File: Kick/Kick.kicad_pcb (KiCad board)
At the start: 4 copper layers, 11 parts, among them J1 CN1 / J11, J2 CN2 / J12, U0 NOIP1SN1300A-QTI, U1 NOIP1SN1300A-QTI, U2 NX3L4053, U3 NX3L4053, U4 MIC5504-1.8YM5

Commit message: acurrate placement of devices, HF impedance calculation
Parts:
- moved U3 12.4 mm to (118.7, 87.6)
- moved U0 11.2 mm to (104.4, 69.4)
- moved U2 10.9 mm to (86.8, 89.4)
- moved U1 9.72 mm to (78.3, 69.4)
- moved J2 2.58 mm to (97.1, 49.2)
- moved J1 2.34 mm to (96.1, 102.2)
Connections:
- J2 pad 22: /clkoutp_0 -> /clkout0_N
- J2 pad 24: /clkoutn_0 -> /clkout0_P
- J2 pad 26: /doutp0_0 -> /dout0_0_N
- J2 pad 28: /doutn0_0 -> /dout0_0_P
- J2 pad 32: /doutp1_0 -> /dout1_0_N
- J2 pad 34: /doutn1_0 -> /dout1_0_P
- J2 pad 36: /doutp2_0 -> /dout2_0_N
- J2 pad 38: /doutn2_0 -> /dout2_0_P
- J2 pad 42: /doutp3_0 -> /dout3_0_N
- J2 pad 44: /doutn3_0 -> /dout3_0_P
- J2 pad 46: /syncp_0 -> /sync0_N
- J2 pad 48: /syncn_0 -> /sync0_P
- J2 pad 52: /clkoutp_1 -> /clkout1_N
- J2 pad 54: /clkoutn_1 -> /clkout1_P
- J2 pad 56: /doutp0_1 -> /dout0_1_N
- J2 pad 58: /doutn0_1 -> /dout0_1_P
- J2 pad 62: /doutp1_1 -> /dout1_1_N
- J2 pad 64: /doutn1_1 -> /dout1_1_P
- J2 pad 66: /doutp2_1 -> /dout2_1_N
- J2 pad 68: /doutn2_1 -> /dout2_1_P
- J2 pad 72: /doutp3_1 -> /dout3_1_N
- J2 pad 74: /doutn3_1 -> /dout3_1_P
- J2 pad 76: /syncp_1 -> /sync1_N
- J2 pad 78: /syncn_1 -> /sync1_P
- U0 pad 10: /doutp0_0 -> /dout0_0_P
- U0 pad 11: /doutn1_0 -> /dout1_0_N
- U0 pad 12: /doutp1_0 -> /dout1_0_P
- U0 pad 13: /doutn2_0 -> /dout2_0_N
- U0 pad 14: /doutp2_0 -> /dout2_0_P
- U0 pad 15: /doutn3_0 -> /dout3_0_N
- U0 pad 16: /doutp3_0 -> /dout3_0_P
- U0 pad 17: /syncn_0 -> /sync0_N
- U0 pad 18: /syncp_0 -> /sync0_P
- U0 pad 46: /resetn_0 -> /reset0_N
- U0 pad 7: /clkoutn_0 -> /clkout0_N
- U0 pad 8: /clkoutp_0 -> /clkout0_P
- U0 pad 9: /doutn0_0 -> /dout0_0_N
- U1 pad 10: /doutp0_1 -> /dout0_1_P
- U1 pad 11: /doutn1_1 -> /dout1_1_N
- U1 pad 12: /doutp1_1 -> /dout1_1_P
- U1 pad 13: /doutn2_1 -> /dout2_1_N
- U1 pad 14: /doutp2_1 -> /dout2_1_P
- U1 pad 15: /doutn3_1 -> /dout3_1_N
- U1 pad 16: /doutp3_1 -> /dout3_1_P
- U1 pad 17: /syncn_1 -> /sync1_N
- U1 pad 18: /syncp_1 -> /sync1_P
- U1 pad 7: /clkoutn_1 -> /clkout1_N
- U1 pad 8: /clkoutp_1 -> /clkout1_P
- U1 pad 9: /doutn0_1 -> /dout0_1_N
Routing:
- net /sync1_P: track 0.00 -> 5.84 mm
- net /sync1_N: track 0.00 -> 5.84 mm

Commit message: calculated new, thinner track widths for 7628 stackup.
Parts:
- moved C1 7.21 mm to (122.1, 72.5)
- moved C2 7.21 mm to (123.5, 68.0)
- moved R1 7.21 mm to (123.5, 70.5)
- moved R2 7.21 mm to (123.5, 73.0)
- moved U4 7.21 mm to (118.9, 66.7)
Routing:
- net /sync1_P: track 5.84 -> 0.00 mm
- net /sync1_N: track 5.84 -> 0.00 mm
- added copper zone on In1.Cu, net GND
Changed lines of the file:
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@@
 	(layers
 		(0 "F.Cu" signal)
-		(1 "In1.Cu" signal)
-		(2 "In2.Cu" signal)
+		(1 "In1.Cu" power)
+		(2 "In2.Cu" power)
 		(31 "B.Cu" signal)
 		(32 "B.Adhes" user "B.Adhesive")
@@
 		(pad_to_mask_clearance 0)
 		(allow_soldermask_bridges_in_footprints no)
-		(grid_origin 70.845 43.925)
+		(grid_origin 65 44)
 		(pcbplotparams
 			(layerselection 0x00010fc_ffffffff)
@@
 	(footprint "Resistor_SMD:R_0603_1608Metric"
 		(layer "B.Cu")
-		(at 130.66 72.52 180)
+		(at 123.47 73.035 180)
 		(descr "Resistor SMD 0603 (1608 Metric), square (rectangular) end terminal, IPC_7351 nominal, (Body size source: IPC-SM-782 page 72, https://www.pcb-3d.com/wordpress/wp-content/uploads/ipc-sm-782a_amendment_1_and_2.pdf), generated with kicad-footprint-generator")
 		(tags "resistor")
@@
 	(footprint "Package_TO_SOT_SMD:SOT-23-5"
 		(layer "B.Cu")
-		(at 126.08 66.135 180)
+		(at 118.89 66.65 180)
 		(descr "SOT, 5 Pin (https://www.jedec.org/sites/default/files/docs/Mo-178c.PDF variant AA), generated with kicad-footprint-generator ipc_gullwing_generator.py")
 		(tags "SOT TO_SOT_SMD")
@@
 	(footprint "Capacitor_SMD:C_0603_1608Metric"
 		(layer "B.Cu")
-		(at 130.66 67.5 180)
+		(at 123.47 68.015 180)
 		(descr "Capacitor SMD 0603 (1608 Metric), square (rectangular) end terminal, IPC_7351 nominal, (Body size source: IPC-SM-782 page 76, https://www.pcb-3d.com/wordpress/wp-content/uploads/ipc-sm-782a_amendment_1_and_2.pdf), generated with kicad-footprint-generator")
 		(tags "capacitor")
@@
 	(footprint "Resistor_SMD:R_0603_1608Metric"
 		(layer "B.Cu")
-		(at 130.66 70.01 180)
+		(at 123.47 70.525 180)
 		(descr "Resistor SMD 0603 (1608 Metric), square (rectangular) end terminal, IPC_7351 nominal, (Body size source: IPC-SM-782 page 72, https://www.pcb-3d.com/wordpress/wp-content/uploads/ipc-sm-782a_amendment_1_and_2.pdf), generated with kicad-footprint-generator")
 		(tags "resistor")
@@
 	(footprint "Capacitor_SMD:C_0603_1608Metric"
 		(layer "B.Cu")
-		(at 129.275 72 180)
+		(at 122.085 72.515 180)
 		(descr "Capacitor SMD 0603 (1608 Metric), square (rectangular) end terminal, IPC_7351 nominal, (Body size source: IPC-SM-782 page 76, https://www.pcb-3d.com/wordpress/wp-content/uploads/ipc-sm-782a_amendment_1_and_2.pdf), generated with kicad-footprint-generator")
 		(tags "capacitor")
@@
 			(at -20.7825 8.985 0)
 			(layer "B.Fab")
+			(hide yes)
 			(effects
 				(font
@@
 		)
 	)
-	(segment
-		(start 74.385 53.017501)
-		(end 74.287 53.115501)
-		(width 0.82)
-		(layer "B.Cu")
-		(net 150)
-	)
-	(segment
-		(start 74.385 50.925)
-		(end 74.385 53.017501)
-		(width 0.82)
-		(layer "B.Cu")
-		(net 150)
-	)
-	(segment
-		(start 74.287 53.115501)
-		(end 74.287 56.725)
-		(width 0.82)
-		(layer "B.Cu")
-		(net 150)
-	)
-	(segment
-		(start 73.115 53.017501)
-		(end 73.213 53.115501)
-		(width 0.82)
-		(layer "B.Cu")
-		(net 158)
-	)
-	(segment
-		(start 73.213 53.115501)
-		(end 73.213 56.725)
-		(width 0.82)
-		(layer "B.Cu")
-		(net 158)
-	)
-	(segment
-		(start 73.115 50.925)
-		(end 73.115 53.017501)
-		(width 0.82)
-		(layer "B.Cu")
-		(net 158)
+	(zone
+		(net 2)
+		(net_name "GND")
+		(layer "In1.Cu")
+		(hatch edge 0.5)
+		(connect_pads
+			(clearance 0.5)
+		)
+		(min_thickness 0.25)
+		(filled_areas_thickness no)
+		(fill yes
+			(thermal_gap 0.5)
+			(thermal_bridge_width 0.5)
+		)
+		(polygon
+			(pts
+				(xy 65 44) (xy 130.8 44) (xy 130.8 107.5) (xy 65 107.5)
+			)
+		)
 	)
 	(zone
@@
 		(polygon
 			(pts
-				(xy 65 44) (xy 135 44) (xy 135 107.5) (xy 65 107.5)
+				(xy 65 44) (xy 130.8 44) (xy 130.8 107.5) (xy 65 107.5)
 			)
 		)

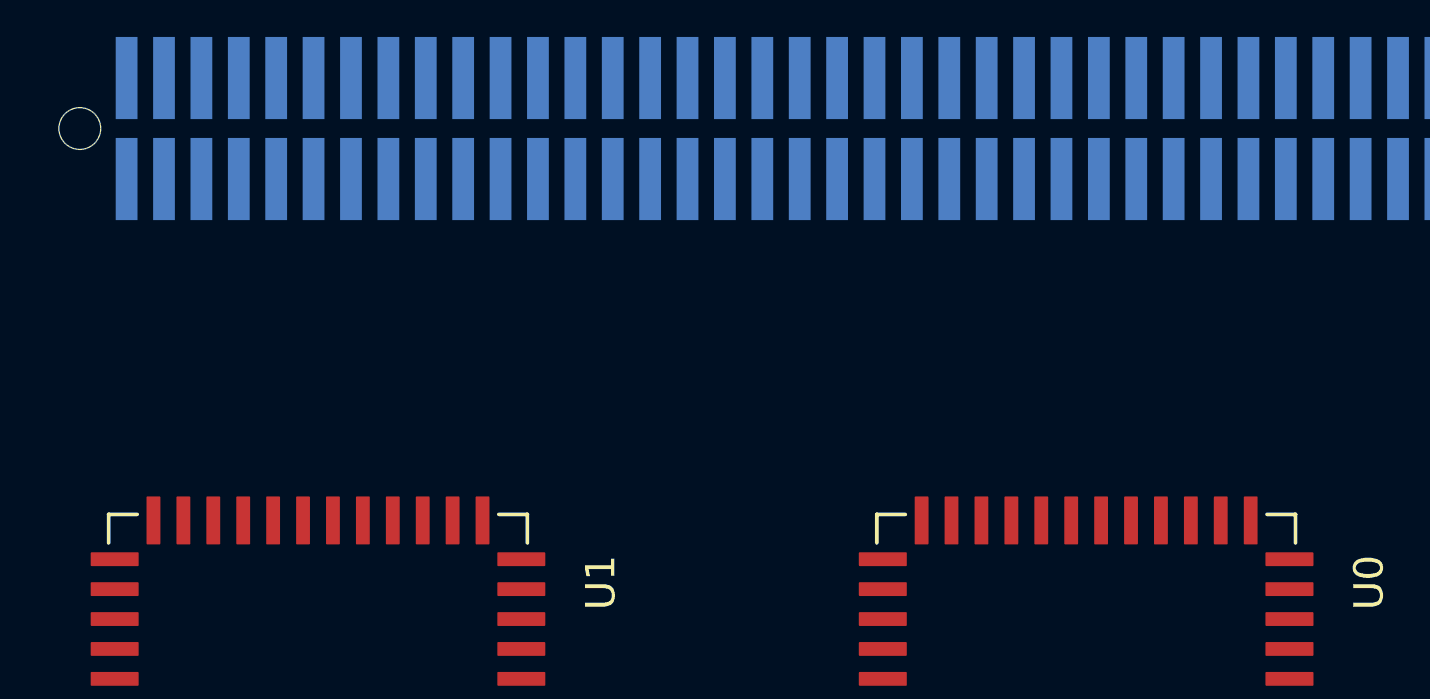
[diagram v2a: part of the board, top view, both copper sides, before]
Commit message: routed lvds pairs, mean skew 0.37mm
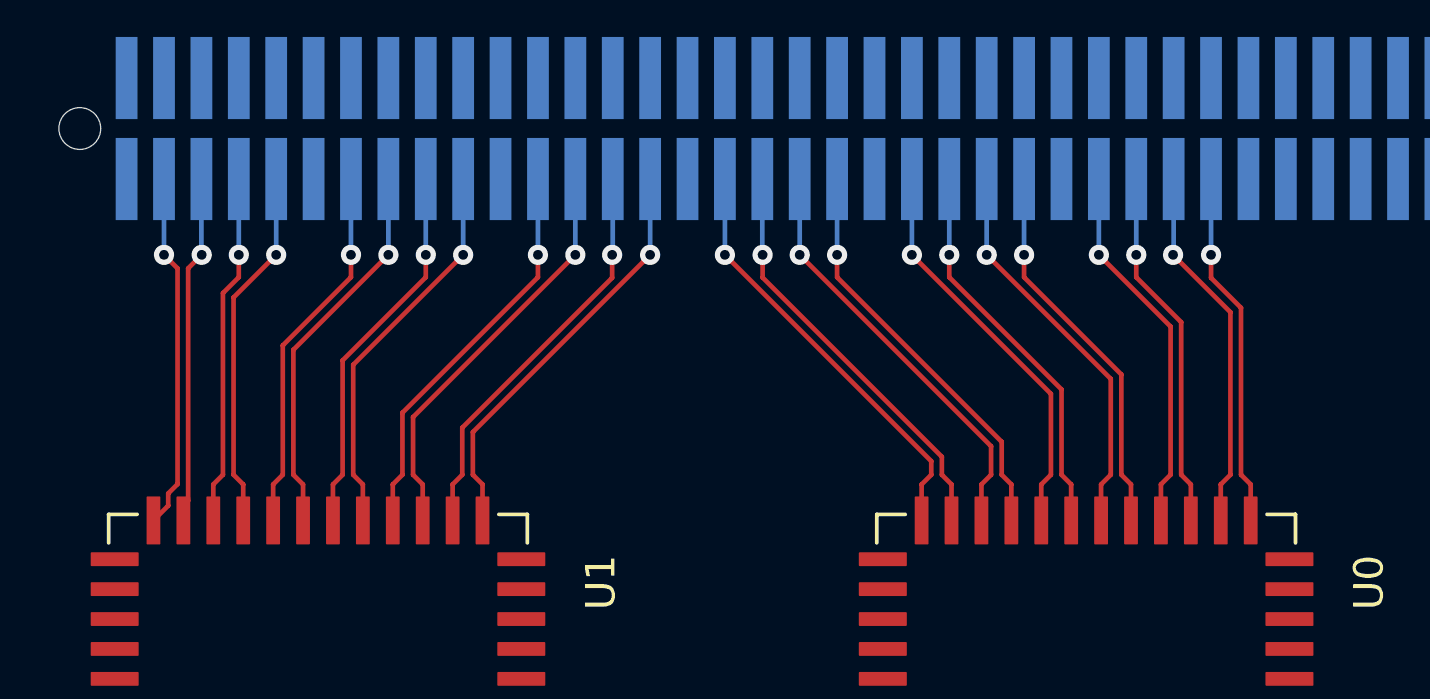
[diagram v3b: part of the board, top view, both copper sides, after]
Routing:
- net /sync0_P: track 0.00 -> 14.6 mm, vias 0 -> 1
- net /dout3_0_P: track 0.00 -> 14.4 mm, vias 0 -> 1
- net /sync0_N: track 0.00 -> 14.3 mm, vias 0 -> 1
- net /clkout1_N: track 0.00 -> 14.2 mm, vias 0 -> 1
- net /dout3_0_N: track 0.00 -> 14.0 mm, vias 0 -> 1
- net /dout0_1_N: track 0.00 -> 14.0 mm, vias 0 -> 1
- net /clkout1_P: track 0.00 -> 13.8 mm, vias 0 -> 1
- net /dout2_0_P: track 0.00 -> 13.7 mm, vias 0 -> 1
- net /dout0_1_P: track 0.00 -> 13.6 mm, vias 0 -> 1
- net /dout1_0_P: track 0.00 -> 13.5 mm, vias 0 -> 1
- net /dout2_0_N: track 0.00 -> 13.3 mm, vias 0 -> 1
- net /dout1_1_N: track 0.00 -> 13.3 mm, vias 0 -> 1
- net /dout1_0_N: track 0.00 -> 13.1 mm, vias 0 -> 1
- net /dout2_1_N: track 0.00 -> 13.1 mm, vias 0 -> 1
- net /dout1_1_P: track 0.00 -> 12.9 mm, vias 0 -> 1
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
